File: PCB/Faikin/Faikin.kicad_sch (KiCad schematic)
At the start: 29 parts, among them J1 1x5, J2 TC2030-USB-NL-DS, J3 Reset, Q1 BSS138PS, U2 ESP32-S3-MINI-1, U3 MD8942

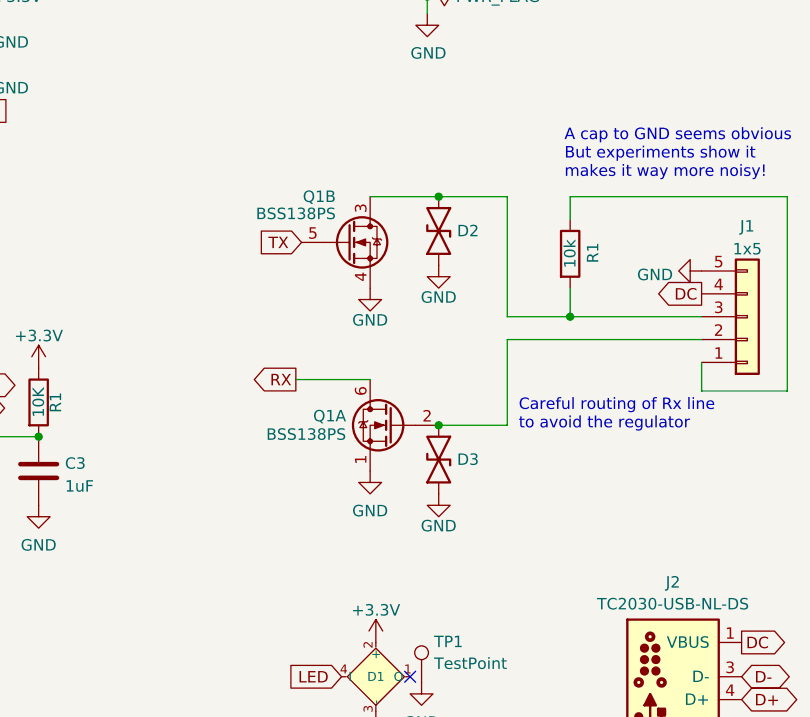
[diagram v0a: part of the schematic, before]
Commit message: 10k pull on rx now - for testing
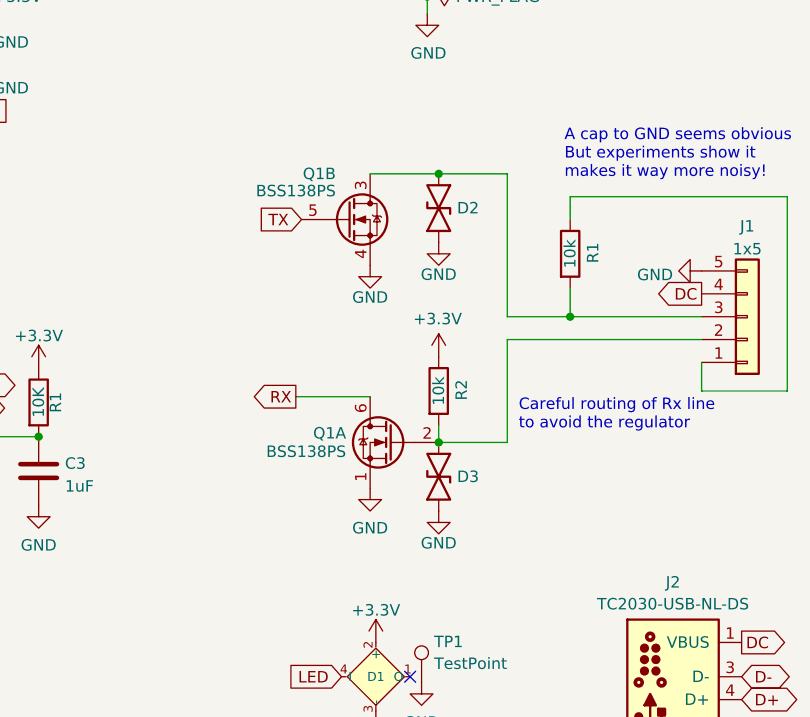
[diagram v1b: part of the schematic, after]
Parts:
- added R2: 10k, RevK:R_0402, symbol Device:R
- TP1: now left out of the parts list
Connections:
- net +3.3V: now also R2.1
- net at D3.2, J1.2 (Pin_2), Q1.2 (GN): now also R2.2
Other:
- moved on the sheet: D2, D3, Q1A, Q1B

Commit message: Added diode
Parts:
- added D4: D, RevK:D_0402, symbol Device:D
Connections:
- net at D3.2, J1.2 (Pin_2), Q1.2 (GN): now also D4.1 (K); no longer R2.2
- new net: D4.2 (A), R2.2
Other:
- moved on the sheet: D1, D2, D3, J2, Q1A, Q1B, R2, TP1

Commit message: Images
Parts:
- renumbered C1 to C2, C2 to C5, C3 to C6, R1 to R3, U2 to U4
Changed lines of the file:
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@@
 (kicad_sch
-	(version 20231120)
+	(version 20241209)
 	(generator "eeschema")
-	(generator_version "8.0")
+	(generator_version "9.0")
 	(paper "A4")
 	(title_block
@@
 		(comment 2 "www.me.uk")
 	)
+	(text "Careful routing of Rx line\nto avoid the regulator"
+		(exclude_from_sim no)
+		(at 175.895 108.585 0)
+		(effects
+			(font
+				(size 1.27 1.27)
+			)
+			(justify left bottom)
+		)
+	)
+	(text "A cap to GND seems obvious\nBut experiments show it\nmakes it way more noisy!"
+		(exclude_from_sim no)
+		(at 180.975 80.645 0)
+		(effects
+			(font
+				(size 1.27 1.27)
+			)
+			(justify left bottom)
+		)
+	)
 	(junction
 		(at 122.555 109.22)
@@
 		)
 	)
-	(text "Careful routing of Rx line\nto avoid the regulator"
-		(exclude_from_sim no)
-		(at 175.895 108.585 0)
-		(effects
-			(font
-				(size 1.27 1.27)
-			)
-			(justify left bottom)
-		)
-	)
-	(text "A cap to GND seems obvious\nBut experiments show it\nmakes it way more noisy!"
-		(exclude_from_sim no)
-		(at 180.975 80.645 0)
-		(effects
-			(font
-				(size 1.27 1.27)
-			)
-			(justify left bottom)
-		)
-	)
 	(global_label "D-"
 		(shape bidirectional)
@@
 		(dnp no)
 		(fields_autoplaced yes)
-		(property "Reference" "#PWR0106"
+		(property "Reference" "#PWR014"
 			(at 122.555 105.41 0)
 			(effects
@@
 		(dnp no)
 		(fields_autoplaced yes)
-		(property "Reference" "#PWR022"
+		(property "Reference" "#PWR023"
 			(at 99.06 145.415 0)
 			(effects
@@
 		(dnp no)
 		(fields_autoplaced yes)
-		(property "Reference" "#PWR01"
+		(property "Reference" "#PWR019"
 			(at 77.47 88.265 0)
 			(effects
@@
 		(dnp no)
 		(fields_autoplaced yes)
-		(property "Reference" "#PWR01"
+		(property "Reference" "#PWR021"
 			(at 77.47 83.185 0)
 			(effects
@@
 		(dnp no)
 		(fields_autoplaced yes)
-		(property "Reference" "#PWR013"
+		(property "Reference" "#PWR011"
 			(at 102.235 45.72 0)
 			(effects
@@
 		(dnp no)
 		(fields_autoplaced yes)
-		(property "Reference" "#PWR0105"
+		(property "Reference" "#PWR015"
 			(at 122.555 123.19 0)
 			(effects
@@
 		(dnp no)
 		(fields_autoplaced yes)
-		(property "Reference" "#PWR03"
+		(property "Reference" "#PWR012"
 			(at 110.49 60.325 0)
 			(effects
@@
 		(dnp no)
 		(fields_autoplaced yes)
-		(property "Reference" "#PWR01"
+		(property "Reference" "#PWR013"
 			(at 120.65 65.405 0)
 			(effects
@@
 		(dnp no)
 		(fields_autoplaced yes)
-		(property "Reference" "C2"
+		(property "Reference" "C5"
 			(at 105.156 34.536 0)
 			(effects
@@
 		(dnp no)
 		(fields_autoplaced yes)
-		(property "Reference" "#PWR01"
+		(property "Reference" "#PWR010"
 			(at 77.47 95.885 0)
 			(effects
@@
 		(dnp no)
 		(fields_autoplaced yes)
-		(property "Reference" "#PWR01"
+		(property "Reference" "#PWR07"
 			(at 77.47 93.345 0)
 			(effects
@@
 		(dnp no)
 		(fields_autoplaced yes)
-		(property "Reference" "#PWR011"
+		(property "Reference" "#PWR05"
 			(at 95.885 45.72 0)
 			(effects
@@
 		(dnp no)
 		(fields_autoplaced yes)
-		(property "Reference" "#PWR04"
+		(property "Reference" "#PWR022"
 			(at 99.06 135.255 0)
 			(effects
@@
 		(dnp no)
 		(fields_autoplaced yes)
-		(property "Reference" "#PWR012"
+		(property "Reference" "#PWR06"
 			(at 102.235 35.56 0)
 			(effects
@@
 		(dnp no)
 		(fields_autoplaced yes)
-		(property "Reference" "C3"
+		(property "Reference" "C6"
 			(at 125.476 112.1953 0)
 			(effects
@@
 		(on_board yes)
 		(dnp no)
-		(property "Reference" "R1"
+		(property "Reference" "R3"
 			(at 124.46 105.41 90)
 			(effects
@@
 		(on_board yes)
 		(dnp no)
-		(property "Reference" "C1"
+		(property "Reference" "C2"
 			(at 86.995 34.147 0)
 			(effects
@@
 		(dnp no)
 		(fields_autoplaced yes)
-		(property "Reference" "U2"
+		(property "Reference" "U4"
 			(at 99.06 48.0782 0)
 			(effects
@@
 		(dnp no)
 		(fields_autoplaced yes)
-		(property "Reference" "#PWR08"
+		(property "Reference" "#PWR04"
 			(at 95.885 35.56 0)
 			(effects
@@
 		(dnp no)
 		(fields_autoplaced yes)
-		(property "Reference" "#PWR01"
+		(property "Reference" "#PWR018"
 			(at 77.47 85.725 0)
 			(effects
@@
 		)
 	)
+	(embedded_fonts no)
 )

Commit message: Clean for new KiCAD
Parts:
- D1: MPN (none) -> C5349953
- D2, D3: MPN (none) -> C5137770
- Q1: JLCPCB Rotation Offset 180 -> (none); LCSC Part # C193381 -> (none); MPN (none) -> C193381
- U3: MPN (none) -> C2684786; Rotation Offset (none) -> 180
- U4: MPN (none) -> C3013941
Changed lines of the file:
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@@
 			)
 		)
+		(property "MPN" "C5137770"
+			(at 163.83 124.46 0)
+			(effects
+				(font
+					(size 1.27 1.27)
+				)
+				(hide yes)
+			)
+		)
 		(pin "2"
 		)
@@
 			)
 		)
+		(property "Sim.Enable" "0"
+			(at 262.255 170.815 0)
+			(effects
+				(font
+					(size 1.27 1.27)
+				)
+				(hide yes)
+			)
+		)
 		(instances
 			(project "Faikin"
@@
 			)
 		)
-		(property "LCSC Part #" "C193381"
+		(property "MPN" "C193381"
 			(at 166.37 70.866 0)
 			(effects
@@
 			)
 		)
-		(property "JLCPCB Rotation Offset" "180"
-			(at 156.845 76.835 0)
-			(effects
-				(font
-					(size 1.27 1.27)
-				)
-				(hide yes)
-			)
-		)
 		(pin "1"
 		)
@@
 			)
 		)
+		(property "Part No" ""
+			(at 186.69 48.26 0)
+			(effects
+				(font
+					(size 1.27 1.27)
+				)
+				(hide yes)
+			)
+		)
+		(property "Note" ""
+			(at 186.69 48.26 0)
+			(effects
+				(font
+					(size 1.27 1.27)
+				)
+				(hide yes)
+			)
+		)
 		(instances
 			(project "Faikin"
@@
 			)
 		)
+		(property "Sim.Enable" "0"
+			(at 259.08 173.99 0)
+			(effects
+				(font
+					(size 1.27 1.27)
+				)
+				(hide yes)
+			)
+		)
 		(instances
 			(project "Faikin"
@@
 			)
 		)
-		(property "Datasheet" " ~"
+		(property "Datasheet" "~"
 			(at 125.73 138.43 0)
 			(effects
@@
 			)
 		)
+		(property "Sim.Enable" "0"
+			(at 262.255 177.165 0)
+			(effects
+				(font
+					(size 1.27 1.27)
+				)
+				(hide yes)
+			)
+		)
 		(instances
 			(project "Faikin"
@@
 			)
 		)
-		(property "Description" ""
+		(property "Description" "Unpolarized capacitor"
 			(at 102.235 35.56 0)
 			(effects
@@
 			)
 		)
+		(property "Sim.Enable" "0"
+			(at 262.255 176.53 0)
+			(effects
+				(font
+					(size 1.27 1.27)
+				)
+				(hide yes)
+			)
+		)
 		(instances
 			(project "Faikin"
@@
 			)
 		)
+		(property "MPN" "C5137770"
+			(at 163.83 75.565 0)
+			(effects
+				(font
+					(size 1.27 1.27)
+				)
+				(hide yes)
+			)
+		)
 		(pin "2"
 		)
@@
 			)
 		)
+		(property "MPN" "C2684786"
+			(at 165.735 75.565 0)
+			(effects
+				(font
+					(size 1.27 1.27)
+				)
+				(hide yes)
+			)
+		)
+		(property "Rotation Offset" "180"
+			(at 165.735 48.895 0)
+			(effects
+				(font
+					(size 1.27 1.27)
+				)
+			)
+		)
 		(pin "1"
 		)
@@
 			)
 		)
-		(property "LCSC Part #" "C193381"
+		(property "MPN" "C193381"
 			(at 152.4 114.681 0)
 			(effects
@@
 			)
 		)
-		(property "JLCPCB Rotation Offset" "180"
-			(at 161.925 120.65 0)
-			(effects
-				(font
-					(size 1.27 1.27)
-				)
-				(hide yes)
-			)
-		)
 		(pin "1"
 		)
@@
 			)
 		)
+		(property "Part No" ""
+			(at 186.69 50.165 0)
+			(effects
+				(font
+					(size 1.27 1.27)
+				)
+				(hide yes)
+			)
+		)
+		(property "Note" ""
+			(at 186.69 50.165 0)
+			(effects
+				(font
+					(size 1.27 1.27)
+				)
+				(hide yes)
+			)
+		)
 		(instances
 			(project "Faikin"
@@
 			)
 		)
+		(property "Sim.Enable" "0"
+			(at 265.43 173.99 0)
+			(effects
+				(font
+					(size 1.27 1.27)
+				)
+				(hide yes)
+			)
+		)
 		(instances
 			(project "Faikin"
@@
 			)
 		)
+		(property "Sim.Enable" "0"
+			(at 262.255 171.45 0)
+			(effects
+				(font
+					(size 1.27 1.27)
+				)
+				(hide yes)
+			)
+		)
 		(instances
 			(project "Faikin"
@@
 			)
 		)
-		(property "Description" ""
+		(property "Description" "Resistor"
 			(at 181.61 88.9 0)
 			(effects
@@
 			)
 		)
+		(property "MPN" "C5349953"
+			(at 100.33 123.825 0)
+			(effects
+				(font
+					(size 1 1)
+				)
+				(justify left top)
+				(hide yes)
+			)
+		)
 		(pin "1"
 		)
@@
 			)
 		)
-		(property "Description" ""
+		(property "Description" "Generic connector, single row, 01x05, script generated (kicad-library-utils/schlib/autogen/connector/)"
 			(at 201.295 95.885 0)
 			(effects
@@
 			)
 		)
-		(property "Description" ""
+		(property "Description" "Resistor"
 			(at 167.005 107.315 0)
 			(effects
@@
 			)
 		)
-		(property "Description" ""
+		(property "Description" "Unpolarized capacitor"
 			(at 122.555 113.03 0)
 			(effects
@@
 			)
 		)
-		(property "Description" ""
+		(property "Description" "Resistor"
 			(at 122.555 105.41 0)
 			(effects
@@
 			)
 		)
-		(property "Description" ""
+		(property "Description" "Unpolarized capacitor"
 			(at 95.885 35.56 0)
 			(effects
@@
 			(at 99.06 114.3 0)
 			(effects
+				(font
+					(size 1.27 1.27)
+				)
+				(hide yes)
+			)
+		)
+		(property "MPN" "C3013941"
+			(at 99.06 114.3 0)
+			(effects

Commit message: PCB Update
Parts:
- C8: LCSC Part # C194427 -> (none); MPN (none) -> C194427
- C9: LCSC Part # C1691 -> (none); MPN (none) -> C1691
- D1: LCSC Part # C5349953 -> (none)
- D2, D3: LCSC Part # C5137770 -> (none)
- D4: LCSC Part # C6341459 -> (none); MPN (none) -> C6341459
- J1: JLCPCB Position Offset 0,-2.61 -> (none); LCSC Part # C265103 -> (none); MPN (none) -> C265103
- U3: LCSC Part # C2684786 -> (none); Rotation Offset 180 -> (none)
- U4: LCSC Part # C3013941 -> (none)
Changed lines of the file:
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@@
 			)
 		)
-		(property "LCSC Part #" "C5137770"
+		(property "MPN" "C5137770"
 			(at 163.83 124.46 0)
 			(effects
@@
 			)
 		)
-		(property "Sim.Enable" "0"
-			(at 262.255 170.815 0)
-			(effects
-				(font
-					(size 1.27 1.27)
-				)
-				(hide yes)
-			)
-		)
 		(instances
 			(project "Faikin"
@@
 			)
 		)
-		(property "Sim.Enable" "0"
-			(at 259.08 173.99 0)
-			(effects
-				(font
-					(size 1.27 1.27)
-				)
-				(hide yes)
-			)
-		)
 		(instances
 			(project "Faikin"
@@
 			)
 		)
-		(property "Sim.Enable" "0"
-			(at 262.255 177.165 0)
-			(effects
-				(font
-					(size 1.27 1.27)
-				)
-				(hide yes)
-			)
-		)
 		(instances
 			(project "Faikin"
@@
 			)
 		)
-		(property "Sim.Enable" "0"
-			(at 262.255 176.53 0)
-			(effects
-				(font
-					(size 1.27 1.27)
-				)
-				(hide yes)
-			)
-		)
 		(instances
 			(project "Faikin"
@@
 			)
 		)
-		(property "LCSC Part #" "C5137770"
+		(property "MPN" "C5137770"
 			(at 163.83 75.565 0)
 			(effects
@@
 			)
 		)
-		(property "LCSC Part #" "C2684786"
-			(at 165.735 75.565 0)
-			(effects
-				(font
-					(size 1.27 1.27)
-				)
-				(hide yes)
-			)
-		)
 		(property "MPN" "C2684786"
 			(at 165.735 75.565 0)
@@
 			)
 		)
-		(property "Rotation Offset" "180"
-			(at 165.735 48.895 0)
-			(effects
-				(font
-					(size 1.27 1.27)
-				)
-			)
-		)
 		(pin "1"
 		)
@@
 			)
 		)
-		(property "Sim.Enable" "0"
-			(at 265.43 173.99 0)
-			(effects
-				(font
-					(size 1.27 1.27)
-				)
-				(hide yes)
-			)
-		)
 		(instances
 			(project "Faikin"
@@
 			)
 		)
-		(property "Sim.Enable" "0"
-			(at 262.255 171.45 0)
-			(effects
-				(font
-					(size 1.27 1.27)
-				)
-				(hide yes)
-			)
-		)
 		(instances
 			(project "Faikin"
@@
 			)
 		)
-		(property "LCSC Part #" "C6341459"
+		(property "MPN" "C6341459"
 			(at 167.005 114.935 0)
 			(effects
@@
 			)
 		)
-		(property "LCSC Part #" "C1691"
+		(property "MPN" "C1691"
 			(at 186.69 44.45 0)
 			(effects
@@
 			)
 		)
-		(property "LCSC Part #" "C5349953"
+		(property "MPN" "C5349953"
 			(at 100.33 123.825 0)
 			(effects
@@
 			)
 		)
-		(property "LCSC Part #" "C265103"
-			(at 201.295 95.885 0)
-			(effects
-				(font
-					(size 1.27 1.27)
-				)
-				(hide yes)
-			)
-		)
-		(property "JLCPCB Position Offset" "0,-2.61"
+		(property "MPN" "C265103"
 			(at 201.295 95.885 0)
 			(effects
@@
 			)
 		)
-		(property "LCSC Part #" "C194427"
+		(property "MPN" "C194427"
 			(at 186.69 42.545 0)
 			(effects
@@
 			)
 		)
-		(property "LCSC Part #" "C3013941"
+		(property "MPN" "C3013941"
 			(at 99.06 114.3 0)
 			(effects

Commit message: Library update
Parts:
- J3: now left out of the parts list
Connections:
- net D-: now also J2.2 (NC), J2.6 (NC)
- net DC: no longer J2.2 (VBUS)
- net GND: no longer J2.6 (GND)
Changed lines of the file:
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@@
 		(unit 1)
 		(exclude_from_sim no)
-		(in_bom yes)
+		(in_bom no)
 		(on_board yes)
 		(dnp no)

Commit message: Diode
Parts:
- D4: MPN C6341459 -> C28642302
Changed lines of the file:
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@@
 (kicad_sch
-	(version 20241209)
+	(version 20250114)
 	(generator "eeschema")
 	(generator_version "9.0")
@@
 			)
 		)
-		(property "MPN" "C6341459"
+		(property "MPN" "C28642302"
 			(at 167.005 114.935 0)
 			(effects

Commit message: Spacing adjust
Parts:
- L2: MPN (none) -> C167879
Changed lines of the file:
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@@
 			)
 		)
-		(property "Part No" ""
-			(at 186.69 53.975 0)
+		(property "MPN" "C167879"
+			(at 186.69 53.975 90)
 			(effects
 				(font
-					(size 1.27 1.27)
-				)
-				(hide yes)
-			)
-		)
-		(property "Note" ""
-			(at 186.69 53.975 0)
-			(effects
-				(font
